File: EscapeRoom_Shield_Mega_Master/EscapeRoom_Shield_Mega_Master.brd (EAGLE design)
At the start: 160 x 100 mm, 24 parts

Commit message: Added all GPIO headers
Placement seems good, but no space for the DFMini on the current layout. Board will have to exceed the footprint of the Mega, but need more additions to justify the space increase.
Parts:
- removed U$10, U$11, U$12, U$13, U$14, U$15, U$16, U$17, U$18, U$19, U$20, U$21, U$22, U$23, U$5, U$6, U$7, U$8, U$9: 1X03, Adam's Parts (work):1X03
- added 1, 10, 11, 12, 13, 14, 15, 16, 17, 18, 19, 2, 20, 21, 22, 23, 24, 25, 26, 27, 28, 29, 3, 30, 31, 32, 33, 34, 35, 36, 37, 38, 39, 4, 40, 41, 42, 43, 44, 45, 46, 47, 48, 49, 5, 50, 51, 52, 53, 6, 7, 8, 9, A1, A10, A11, A12, A13, A14, A15, A2, A3, A4, A5, A6, A7, A8, A9: 1X03, Adam's Parts (work):1X03
- U$4: value 1X03 -> TERMINAL_BLOCK_3P; device Adam's Parts (work):1X03 -> Adam's Parts (work):H3-5.0-15.5X8.0MM
- moved U$3 104.8 mm to (-26.7, 48.3)
- moved U$4 74.1 mm to (-5.08, 12.7)
- moved B1 55.9 mm to (39.4, 26.7)
- moved U$1 12.7 mm to (-1.27, 43.2)
- moved U$2 8.52 mm to (12.7, 12.7), turned to 0 degrees
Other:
- board size 160 x 100 mm -> 98.4 x 53.5 mm

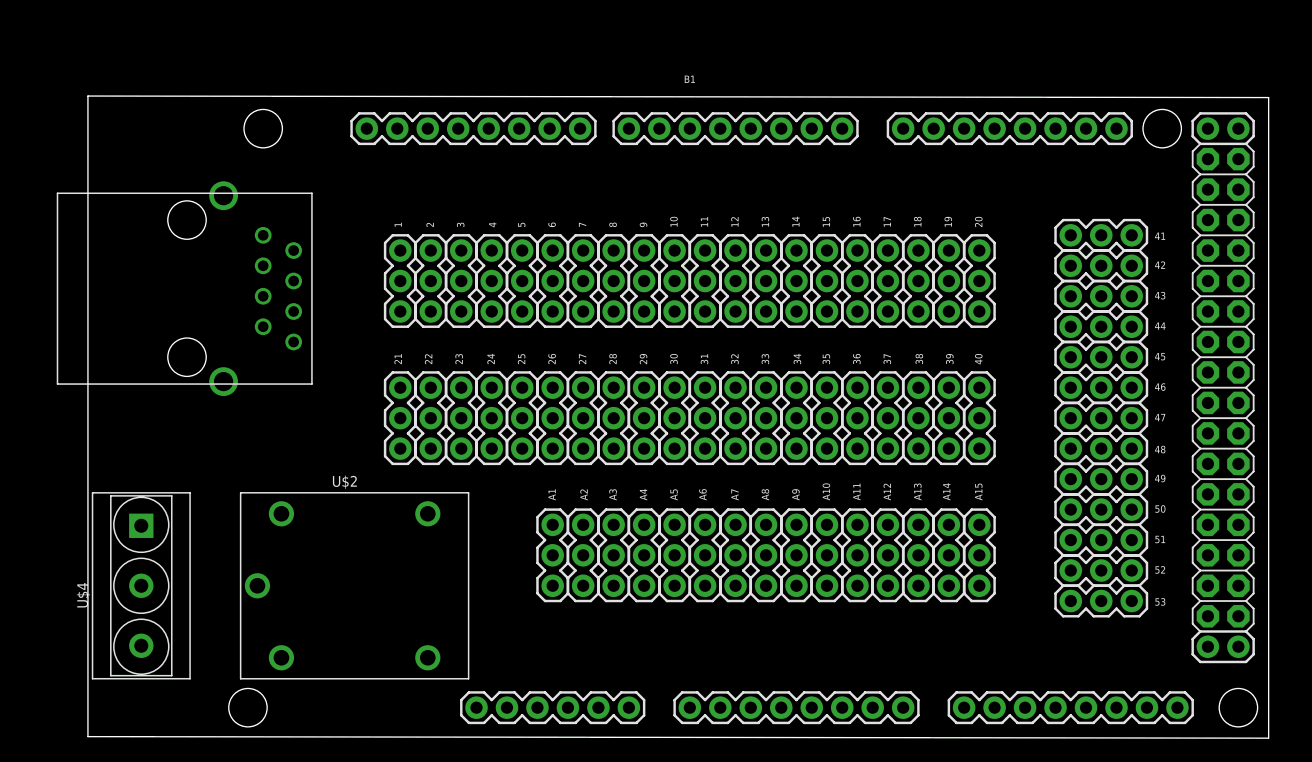
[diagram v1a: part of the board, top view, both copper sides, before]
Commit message: Finished defining pin breakouts, wiring pins
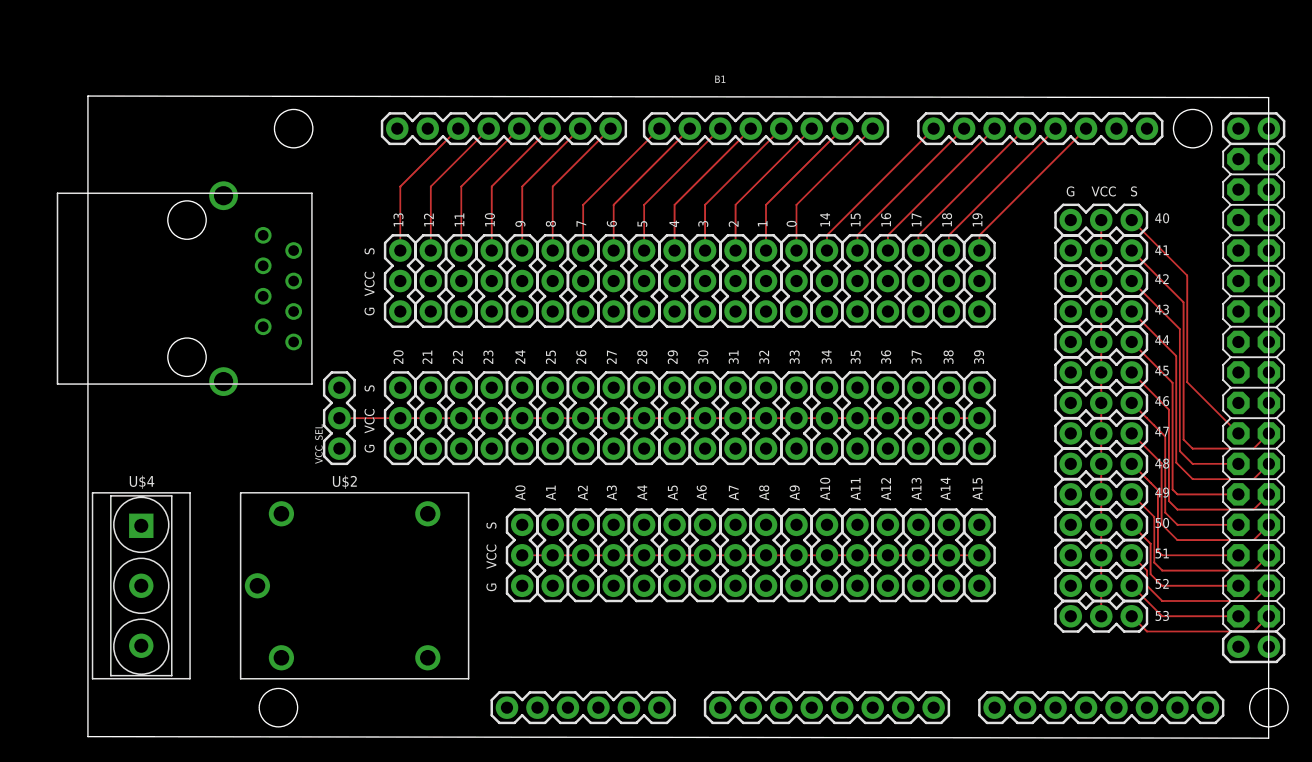
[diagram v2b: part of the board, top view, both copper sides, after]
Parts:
- added 0, A0, VCC_SEL: 1X03, Adam's Parts (work):1X03
- moved 20 49.6 mm to (16.5, 24.1)
- moved 1 30.5 mm to (47.0, 35.6)
- moved 13 30.5 mm to (16.5, 35.6)
- moved 12 25.4 mm to (19.1, 35.6)
- moved 2 25.4 mm to (44.5, 35.6)
- moved 40 20.5 mm to (72.4, 43.2), turned to 0 degrees
- moved 11 20.3 mm to (21.6, 35.6)
- moved 3 20.3 mm to (41.9, 35.6)
- moved 10 15.2 mm to (24.1, 35.6)
- moved 4 15.2 mm to (39.4, 35.6)
- moved 5 10.2 mm to (36.8, 35.6)
- moved 9 10.2 mm to (26.7, 35.6)
- moved 6 5.08 mm to (34.3, 35.6)
- moved 8 5.08 mm to (29.2, 35.6)
- moved 31 2.54 mm to (44.5, 24.1)
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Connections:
- new net 0: 0.3, B1.0
- new net 1: 1.3, B1.1
- new net 10: 10.3, B1.10
- new net 11: 11.3, B1.11
- new net 12: 12.3, B1.12
- new net 12V: B1.VIN
- new net 13: 13.3, B1.13
- new net 14: 14.3, B1.14
- new net 15: 15.3, B1.15
- new net 16: 16.3, B1.16
- new net 17: 17.3, B1.17
- new net 18: 18.3, B1.18
- new net 19: 19.3, B1.19
- new net 2: 2.3, B1.2
- new net 20: 20.3, B1.20
- new net 21: 21.3, B1.21
- new net 22: 22.3, B1.22
- new net 23: 23.3, B1.23
- new net 24: 24.3, B1.24
- new net 25: 25.3, B1.25
- new net 26: 26.3, B1.26
- new net 27: 27.3, B1.27
- new net 28: 28.3, B1.28
- new net 29: 29.3, B1.29
- new net 3: 3.3, B1.3
- new net 3.3V: B1.3.3V, VCC_SEL.1
- new net 30: 30.3, B1.30
- new net 31: 31.3, B1.31
- new net 32: 32.3, B1.32
- new net 33: 33.3, B1.33
- new net 34: 34.3, B1.34
- new net 35: 35.3, B1.35
- new net 36: 36.3, B1.36
- new net 37: 37.3, B1.37
- new net 38: 38.3, B1.38
- new net 39: 39.3, B1.39
- new net 4: 4.3, B1.4
- new net 40: 40.3, B1.40
- new net 41: 41.3, B1.41
- new net 42: 42.3, B1.42
- new net 43: 43.3, B1.43
- new net 44: 44.3, B1.44
- new net 45: 45.3, B1.45
- new net 46: 46.3, B1.46
- new net 47: 47.3, B1.47
- new net 48: 48.3, B1.48
- new net 49: 49.3, B1.49
- new net 5: 5.3, B1.5
- new net 50: 50.3, B1.50
- new net 51: 51.3, B1.51
- new net 52: 52.3, B1.52
- new net 53: 53.3, B1.53
- new net 5V: B1.5V@0, B1.5V@1, B1.5V@2, VCC_SEL.3
- new net 6: 6.3, B1.6
- new net 7: 7.3, B1.7
- new net 8: 8.3, B1.8
- new net 9: 9.3, B1.9
- new net A0: A0.3, B1.A0
- new net A1: A1.3, B1.A1
- new net A10: A10.3, B1.A10
- new net A11: A11.3, B1.A11
- new net A12: A12.3, B1.A12
- new net A13: A13.3, B1.A13
- new net A14: A14.3, B1.A14
- new net A15: A15.3, B1.A15
- new net A2: A2.3, B1.A2
- new net A3: A3.3, B1.A3
- new net A4: A4.3, B1.A4
- new net A5: A5.3, B1.A5
- new net A6: A6.3, B1.A6
- new net A7: A7.3, B1.A7
- new net A8: A8.3, B1.A8
- new net A9: A9.3, B1.A9
- new net GND: 0.1, 1.1, 10.1, 11.1, 12.1, 13.1, 14.1, 15.1, 16.1, 17.1, 18.1, 19.1, 2.1, 20.1, 21.1, 22.1, 23.1, 24.1, 25.1, 26.1, 27.1, 28.1, 29.1, 3.1, 30.1, 31.1, 32.1, 33.1, 34.1, 35.1, 36.1, 37.1, 38.1, 39.1, 4.1, 40.1, 41.1, 42.1, 43.1, 44.1, 45.1, 46.1, 47.1, 48.1, 49.1, 5.1, 50.1, 51.1, 52.1, 53.1, 6.1, 7.1, 8.1, 9.1, A0.1, A1.1, A10.1, A11.1, A12.1, A13.1, A14.1, A15.1, A2.1, A3.1, A4.1, A5.1, A6.1, A7.1, A8.1, A9.1, B1.GND@0, B1.GND@1, B1.GND@2, B1.GND@3, B1.GND@4
- new net VCC: 0.2, 1.2, 10.2, 11.2, 12.2, 13.2, 14.2, 15.2, 16.2, 17.2, 18.2, 19.2, 2.2, 20.2, 21.2, 22.2, 23.2, 24.2, 25.2, 26.2, 27.2, 28.2, 29.2, 3.2, 30.2, 31.2, 32.2, 33.2, 34.2, 35.2, 36.2, 37.2, 38.2, 39.2, 4.2, 40.2, 41.2, 42.2, 43.2, 44.2, 45.2, 46.2, 47.2, 48.2, 49.2, 5.2, 50.2, 51.2, 52.2, 53.2, 6.2, 7.2, 8.2, 9.2, A0.2, A1.2, A10.2, A11.2, A12.2, A13.2, A14.2, A15.2, A2.2, A3.2, A4.2, A5.2, A6.2, A7.2, A8.2, A9.2, VCC_SEL.2
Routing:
- net VCC: track 0.00 -> 124.5 mm
- net 41: track 0.00 -> 25.5 mm
- net 43: track 0.00 -> 23.0 mm
- net 40: track 0.00 -> 21.5 mm
- net 45: track 0.00 -> 21.2 mm
- net 42: track 0.00 -> 21.2 mm
- net 44: track 0.00 -> 19.4 mm
- net 47: track 0.00 -> 18.6 mm
- net 49: track 0.00 -> 16.8 mm
- net 46: track 0.00 -> 16.8 mm
- net 48: track 0.00 -> 15.0 mm
- net 51: track 0.00 -> 14.3 mm
- net 18: track 0.00 -> 13.8 mm
- net 16: track 0.00 -> 13.8 mm
- net 19: track 0.00 -> 13.8 mm
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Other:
- board text added: "G"
- board text added: "S"
- board text added: "VCC"

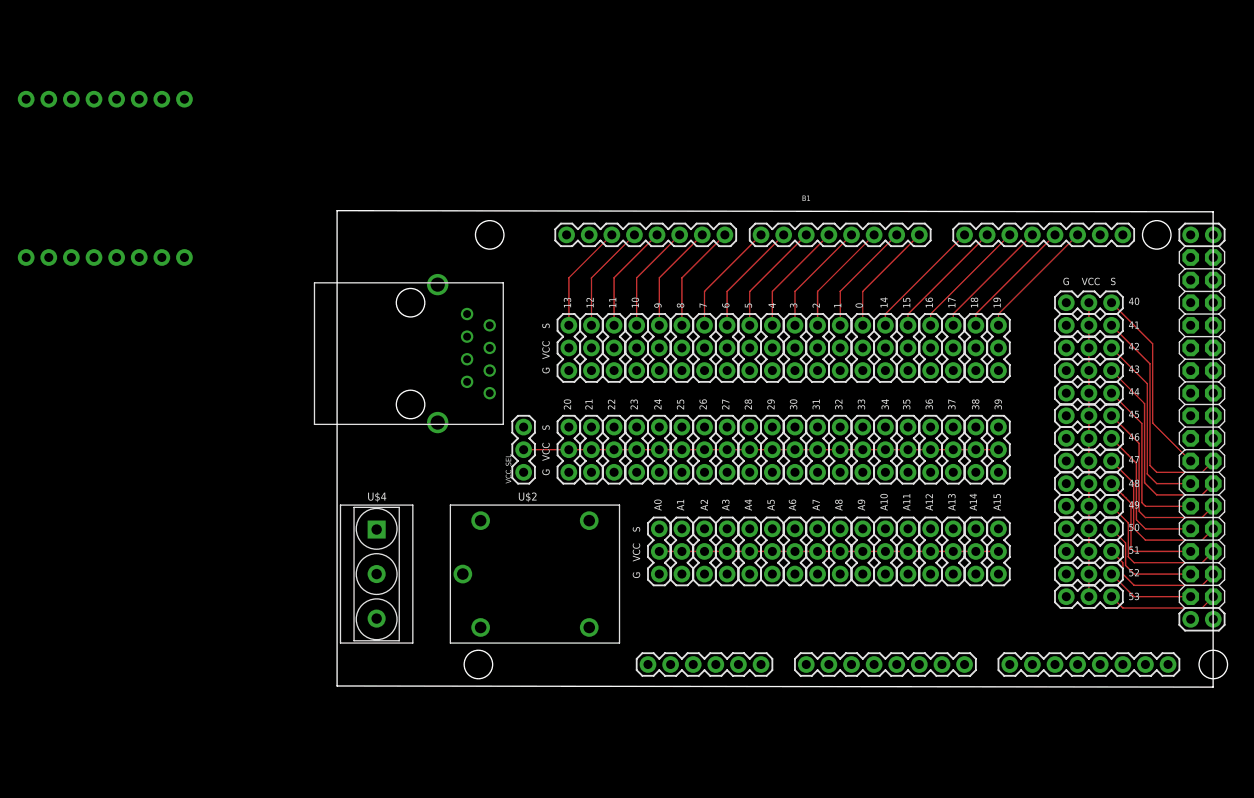
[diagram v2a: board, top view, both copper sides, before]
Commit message: Changed DFMini TX/RX pins to compatible pins. Removed R1. Labeled 12V out terminal blocks.
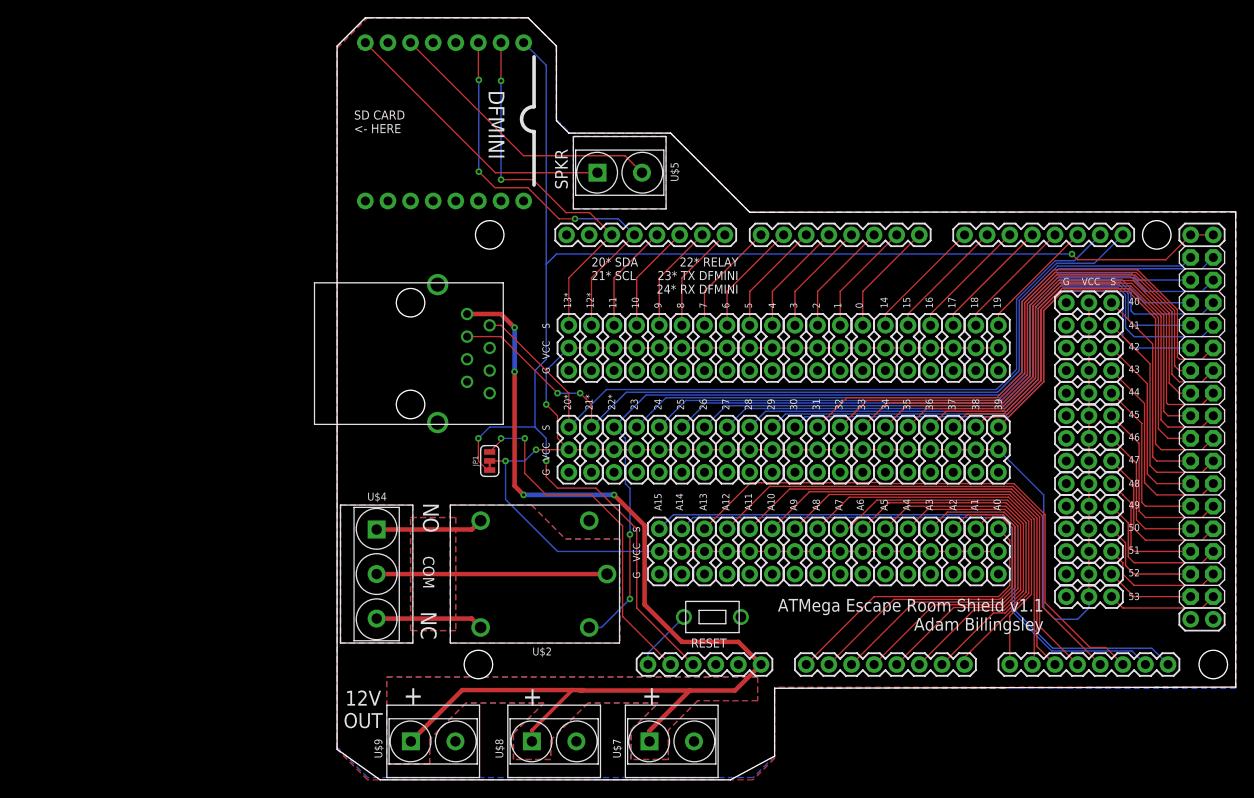
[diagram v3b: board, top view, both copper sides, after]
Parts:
- removed VCC_SEL: 1X03, Adam's Parts (work):1X03
- added JP1: JUMPER-SMT_3_1-NC_TRACE_SILK, SparkFun-Jumpers:SMT-JUMPER_3_1-NC_TRACE_SILK
- added U$5, U$7, U$8, U$9: TERMINAL_BLOCK_2P, Adam's Parts (work):H2-5.0-10.5X8.0MM
- added U$6: BUTTON_PTS636_SL50_LFS, Adam's Parts (work):BUTTON_PTS636_SL50_LFS
- moved U$3 38.6 mm to (11.4, 54.6)
- moved A0 38.1 mm to (64.8, 12.7)
- moved A15 38.1 mm to (26.7, 12.7)
- moved A1 33.0 mm to (62.2, 12.7)
- moved A14 33.0 mm to (29.2, 12.7)
- moved A13 27.9 mm to (31.8, 12.7)
- moved A2 27.9 mm to (59.7, 12.7)
- moved A12 22.9 mm to (34.3, 12.7)
- moved A3 22.9 mm to (57.1, 12.7)
- moved A11 17.8 mm to (36.8, 12.7)
- moved A4 17.8 mm to (54.6, 12.7)
- moved A10 12.7 mm to (39.4, 12.7)
- moved A5 12.7 mm to (52.1, 12.7)
- moved A6 7.62 mm to (49.5, 12.7)
- moved A9 7.62 mm to (41.9, 12.7)
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- renumbered 12 to 12*, 13 to 13*, 20 to 20*, 21 to 21*, 22 to 22*
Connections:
- new net N$1: U$2.1, U$4.2
- new net N$2: U$2.4, U$4.1
- new net N$3: U$2.5, U$4.3
- new net N$5: U$3.P$16, U$5.1
- new net N$6: U$3.P$14, U$5.2
- new net N$7: B1.RESET, U$6.P$2
- net 12: now also U$3.P$11
- net 12V: now also U$1.P$1, U$7.1, U$8.1, U$9.1
- net 13: now also U$3.P$10
- net 20: now also U$1.P$2
- net 21: now also U$1.P$3
- net 22: now also U$2.3
- net 3.3V: now also JP1.1; no longer VCC_SEL.1
- net 5V: now also JP1.3, U$3.P$9; no longer VCC_SEL.3
- net GND: now also U$1.P$10, U$1.P$8, U$1.P$9, U$2.2, U$3.P$15, U$3.P$7, U$6.P$1, U$7.2, U$8.2, U$9.2
- net VCC: now also JP1.2; no longer VCC_SEL.2
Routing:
- net 5V: track 0.00 -> 169.0 mm, vias 0 -> 3
- net 12V: track 0.00 -> 123.5 mm, vias 0 -> 4
- net VCC: track 124.5 -> 242.2 mm, vias 0 -> 3
- net 22: track 0.00 -> 103.2 mm, vias 0 -> 2
- net 21: track 0.00 -> 92.9 mm, vias 0 -> 2
- net 20: track 0.00 -> 89.1 mm
- net 23: track 0.00 -> 77.3 mm
- net 25: track 0.00 -> 72.5 mm
- net 24: track 0.00 -> 71.7 mm
- net A15: track 0.00 -> 70.3 mm
- net 27: track 0.00 -> 69.2 mm
- net 26: track 0.00 -> 67.2 mm
- net 29: track 0.00 -> 65.7 mm
- net A14: track 0.00 -> 64.9 mm
- net 28: track 0.00 -> 64.4 mm
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- added copper zone on layer 1, net GND
- added copper zone on layer 16, net GND
- added copper zone on layer 1, net NOGND
- added copper zone on layer 16, net NOGND
- added copper zone on layer 1, net NOGND1
- added copper zone on layer 16, net NOGND1
- added copper zone on layer 1, net NOGND2
- added copper zone on layer 16, net NOGND2
- added copper zone on layer 1, net NOGND3
- added copper zone on layer 16, net NOGND3
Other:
- board size 98.4 x 53.5 mm -> 100.9 x 85.6 mm
- board text added: "+"
- board text added: "12V OUT"
- board text added: "20* SDA 21* SCL"
- board text added: "22* RELAY 23* TX DFMINI 24* RX DFMINI"
- board text added: "ATMega Escape Room Shield v1.1 Adam Billingsley"
- board text added: "COM"
- board text added: "DFMINI"
- board text added: "NC"
- board text added: "NO"
- board text added: "RESET"
- board text added: "SD CARD <- HERE"
- board text added: "SPKR"
